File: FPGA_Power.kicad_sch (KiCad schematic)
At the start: 13 parts, among them U5 NCP115AMX120TCG, U9 ICE40UP5K-SG48ITR

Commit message: Fixed a lot more mistakes...
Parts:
- added TP28: 1V2, TestPoint:TestPoint_THTPad_D2.5mm_Drill1.2mm, symbol Connector:TestPoint
- U5: Price (none) -> $0.30
- U9: Price (none) -> $0.09
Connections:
- net +1V2: now also TP28.1
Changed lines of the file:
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@@
 			)
 		)
-		(property "Price" ""
+		(property "Price" "$0.30"
 			(at 111.76 86.36 0)
 			(hide yes)
@@
 			)
 		)
+		(property "Field21" ""
+			(at 111.76 86.36 0)
+			(hide yes)
+			(show_name no)
+			(do_not_autoplace no)
+			(effects
+				(font
+					(size 1.27 1.27)
+				)
+			)
+		)
 		(pin "1"
 		)
@@
 	)
 	(symbol
+		(lib_id "Connector:TestPoint")
+		(at 146.05 76.2 90)
+		(unit 1)
+		(body_style 1)
+		(exclude_from_sim no)
+		(in_bom yes)
+		(on_board yes)
+		(in_pos_files yes)
+		(dnp no)
+		(property "Reference" "TP28"
+			(at 139.7 76.2 90)
+			(hide yes)
+			(show_name no)
+			(do_not_autoplace no)
+			(effects
+				(font
+					(size 1.27 1.27)
+				)
+				(justify left)
+			)
+		)
+		(property "Value" "1V2"
+			(at 143.51 78.74 90)
+			(show_name no)
+			(do_not_autoplace no)
+			(effects
+				(font
+					(size 1.27 1.27)
+				)
+				(justify left)
+			)
+		)
+		(property "Footprint" "TestPoint:TestPoint_THTPad_D2.5mm_Drill1.2mm"
+			(at 146.05 71.12 0)
+			(hide yes)
+			(show_name no)
+			(do_not_autoplace no)
+			(effects
+				(font
+					(size 1.27 1.27)
+				)
+			)
+		)
+		(property "Datasheet" ""
+			(at 146.05 71.12 0)
+			(hide yes)
+			(show_name no)
+			(do_not_autoplace no)
+			(effects
+				(font
+					(size 1.27 1.27)
+				)
+			)
+		)
+		(property "Description" ""
+			(at 146.05 76.2 0)
+			(hide yes)
+			(show_name no)
+			(do_not_autoplace no)
+			(effects
+				(font
+					(size 1.27 1.27)
+				)
+			)
+		)
+		(property "JLCPCB #" ""
+			(at 146.05 76.2 0)
+			(hide yes)
+			(show_name no)
+			(do_not_autoplace no)
+			(effects
+				(font
+					(size 1.27 1.27)
+				)
+			)
+		)
+		(pin "1"
+		)
+		(instances
+			(project "DDC_SDR"
+				(path "/7dfef218-ca21-47b0-a8d3-67c7d55cb9d2/2ce56689-3987-4b0d-b06d-53c251a2345f"
+					(reference "TP28")
+					(unit 1)
+				)
+			)
+		)
+	)
+	(symbol
 		(lib_id "UPduino_v3.0:power_GND")
 		(at 182.88 100.33 0)
@@
 			)
 		)
-		(property "Price" ""
+		(property "Price" "$0.09"
 			(at 212.09 106.68 90)
 			(hide yes)

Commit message: Fixing more errors....
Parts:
- renumbered U9 to U7
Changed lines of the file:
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@@
 		(in_pos_files yes)
 		(dnp no)
-		(property "Reference" "U9"
+		(property "Reference" "U7"
 			(at 212.09 97.3582 90)
 			(show_name no)
@@
 			(project "DDC_SDR"
 				(path "/7dfef218-ca21-47b0-a8d3-67c7d55cb9d2/2ce56689-3987-4b0d-b06d-53c251a2345f"
-					(reference "U9")
+					(reference "U7")
 					(unit 4)
 				)

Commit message: Minor tweaks...
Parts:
- U7: Price $0.09 -> $8.49
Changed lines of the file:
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@@
 			)
 		)
-		(property "Price" "$0.09"
+		(property "Price" "$8.49"
 			(at 212.09 106.68 90)
 			(hide yes)

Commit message: Starting to place components
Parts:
- JP1: footprint (none) -> Jumper:SolderJumper-2_P1.3mm_Bridged_RoundedPad1.0x1.5mm
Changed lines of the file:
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@@
 			)
 		)
-		(property "Footprint" ""
+		(property "Footprint" "Jumper:SolderJumper-2_P1.3mm_Bridged_RoundedPad1.0x1.5mm"
 			(at 154.94 92.71 0)
 			(hide yes)

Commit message: AF DAC Some VDDA Placed
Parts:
- renumbered C62 to C70, C61 to C71, C54 to C72, C39 to C73, C60 to C74, C33 to C75, C51 to C76, C56 to C77, D5 to D8, JP1 to JP7, R12 to R54, TP28 to TP9, U5 to U11
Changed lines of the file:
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@@
 		(in_pos_files yes)
 		(dnp no)
-		(property "Reference" "#PWR092"
+		(property "Reference" "#PWR0138"
 			(at 185.42 90.17 0)
 			(hide yes)
@@
 			(project "DDC_SDR"
 				(path "/7dfef218-ca21-47b0-a8d3-67c7d55cb9d2/2ce56689-3987-4b0d-b06d-53c251a2345f"
-					(reference "#PWR092")
+					(reference "#PWR0138")
 					(unit 1)
 				)
@@
 		(dnp no)
 		(fields_autoplaced yes)
-		(property "Reference" "U5"
+		(property "Reference" "U11"
 			(at 111.76 77.47 0)
 			(show_name no)
@@
 			(project "DDC_SDR"
 				(path "/7dfef218-ca21-47b0-a8d3-67c7d55cb9d2/2ce56689-3987-4b0d-b06d-53c251a2345f"
-					(reference "U5")
+					(reference "U11")
 					(unit 1)
 				)
@@
 		(in_pos_files yes)
 		(dnp no)
-		(property "Reference" "#PWR097"
+		(property "Reference" "#PWR0139"
 			(at 223.52 114.3 0)
 			(hide yes)
@@
 			(project "DDC_SDR"
 				(path "/7dfef218-ca21-47b0-a8d3-67c7d55cb9d2/2ce56689-3987-4b0d-b06d-53c251a2345f"
-					(reference "#PWR097")
+					(reference "#PWR0139")
 					(unit 1)
 				)
@@
 		(dnp no)
 		(fields_autoplaced yes)
-		(property "Reference" "C33"
+		(property "Reference" "C75"
 			(at 176.53 77.4699 0)
 			(show_name no)
@@
 			(project "DDC_SDR"
 				(path "/7dfef218-ca21-47b0-a8d3-67c7d55cb9d2/2ce56689-3987-4b0d-b06d-53c251a2345f"
-					(reference "C33")
+					(reference "C75")
 					(unit 1)
 				)
@@
 		(in_pos_files yes)
 		(dnp no)
-		(property "Reference" "#PWR090"
+		(property "Reference" "#PWR0136"
 			(at 173.99 90.17 0)
 			(hide yes)
@@
 			(project "DDC_SDR"
 				(path "/7dfef218-ca21-47b0-a8d3-67c7d55cb9d2/2ce56689-3987-4b0d-b06d-53c251a2345f"
-					(reference "#PWR090")
+					(reference "#PWR0136")
 					(unit 1)
 				)
@@
 		(dnp no)
 		(fields_autoplaced yes)
-		(property "Reference" "C61"
+		(property "Reference" "C71"
 			(at 125.73 85.0899 0)
 			(show_name no)
@@
 			(project "DDC_SDR"
 				(path "/7dfef218-ca21-47b0-a8d3-67c7d55cb9d2/2ce56689-3987-4b0d-b06d-53c251a2345f"
-					(reference "C61")
+					(reference "C71")
 					(unit 1)
 				)
@@
 		(in_pos_files yes)
 		(dnp no)
-		(property "Reference" "#PWR085"
+		(property "Reference" "#PWR0133"
 			(at 157.48 130.81 0)
 			(hide yes)
@@
 			(project "DDC_SDR"
 				(path "/7dfef218-ca21-47b0-a8d3-67c7d55cb9d2/2ce56689-3987-4b0d-b06d-53c251a2345f"
-					(reference "#PWR085")
+					(reference "#PWR0133")
 					(unit 1)
 				)
@@
 		(dnp no)
 		(fields_autoplaced yes)
-		(property "Reference" "C54"
+		(property "Reference" "C72"
 			(at 160.02 118.1099 0)
 			(show_name no)
@@
 			(project "DDC_SDR"
 				(path "/7dfef218-ca21-47b0-a8d3-67c7d55cb9d2/2ce56689-3987-4b0d-b06d-53c251a2345f"
-					(reference "C54")
+					(reference "C72")
 					(unit 1)
 				)
@@
 		(dnp no)
 		(fields_autoplaced yes)
-		(property "Reference" "C62"
+		(property "Reference" "C70"
 			(at 99.06 92.7099 0)
 			(show_name no)
@@
 			(project "DDC_SDR"
 				(path "/7dfef218-ca21-47b0-a8d3-67c7d55cb9d2/2ce56689-3987-4b0d-b06d-53c251a2345f"
-					(reference "C62")
+					(reference "C70")
 					(unit 1)
 				)
@@
 		(in_pos_files yes)
 		(dnp no)
-		(property "Reference" "TP28"
+		(property "Reference" "TP9"
 			(at 139.7 76.2 90)
 			(hide yes)
@@
 			(project "DDC_SDR"
 				(path "/7dfef218-ca21-47b0-a8d3-67c7d55cb9d2/2ce56689-3987-4b0d-b06d-53c251a2345f"
-					(reference "TP28")
+					(reference "TP9")
 					(unit 1)
 				)
@@
 		(in_pos_files yes)
 		(dnp no)
-		(property "Reference" "#PWR091"
+		(property "Reference" "#PWR0137"
 			(at 182.88 106.68 0)
 			(hide yes)
@@
 			(project "DDC_SDR"
 				(path "/7dfef218-ca21-47b0-a8d3-67c7d55cb9d2/2ce56689-3987-4b0d-b06d-53c251a2345f"
-					(reference "#PWR091")
+					(reference "#PWR0137")
 					(unit 1)
 				)
@@
 		(in_pos_files yes)
 		(dnp no)
-		(property "Reference" "#PWR087"
+		(property "Reference" "#PWR0135"
 			(at 172.72 130.81 0)
 			(hide yes)
@@
 			(project "DDC_SDR"
 				(path "/7dfef218-ca21-47b0-a8d3-67c7d55cb9d2/2ce56689-3987-4b0d-b06d-53c251a2345f"
-					(reference "#PWR087")
+					(reference "#PWR0135")
 					(unit 1)
 				)
@@
 		(in_pos_files yes)
 		(dnp no)
-		(property "Reference" "#PWR014"
+		(property "Reference" "#PWR0128"
 			(at 96.52 105.41 0)
 			(hide yes)
@@
 			(project "DDC_SDR"
 				(path "/7dfef218-ca21-47b0-a8d3-67c7d55cb9d2/2ce56689-3987-4b0d-b06d-53c251a2345f"
-					(reference "#PWR014")
+					(reference "#PWR0128")
 					(unit 1)
 				)
@@
 		(dnp no)
 		(fields_autoplaced yes)
-		(property "Reference" "C39"
+		(property "Reference" "C73"
 			(at 175.26 93.9799 0)
 			(show_name no)
@@
 			(project "DDC_SDR"
 				(path "/7dfef218-ca21-47b0-a8d3-67c7d55cb9d2/2ce56689-3987-4b0d-b06d-53c251a2345f"
-					(reference "C39")
+					(reference "C73")
 					(unit 1)
 				)
@@
 		(dnp no)
 		(fields_autoplaced yes)
-		(property "Reference" "C56"
+		(property "Reference" "C77"
 			(at 187.96 77.4699 0)
 			(show_name no)
@@
 			(project "DDC_SDR"
 				(path "/7dfef218-ca21-47b0-a8d3-67c7d55cb9d2/2ce56689-3987-4b0d-b06d-53c251a2345f"
-					(reference "C56")
+					(reference "C77")
 					(unit 1)
 				)
@@
 		(dnp no)
 		(fields_autoplaced yes)
-		(property "Reference" "C51"
+		(property "Reference" "C76"
 			(at 185.42 93.9799 0)
 			(show_name no)
@@
 			(project "DDC_SDR"
 				(path "/7dfef218-ca21-47b0-a8d3-67c7d55cb9d2/2ce56689-3987-4b0d-b06d-53c251a2345f"
-					(reference "C51")
+					(reference "C76")
 					(unit 1)
 				)
@@
 		(in_pos_files yes)
 		(dnp no)
-		(property "Reference" "#PWR086"
+		(property "Reference" "#PWR0134"
 			(at 172.72 106.68 0)
 			(hide yes)
@@
 			(project "DDC_SDR"
 				(path "/7dfef218-ca21-47b0-a8d3-67c7d55cb9d2/2ce56689-3987-4b0d-b06d-53c251a2345f"
-					(reference "#PWR086")
+					(reference "#PWR0134")
 					(unit 1)
 				)
@@
 		(in_pos_files yes)
 		(dnp no)
-		(property "Reference" "#PWR0113"
+		(property "Reference" "#PWR0127"
 			(at 96.52 86.36 0)
 			(hide yes)
@@
 			(project "DDC_SDR"
 				(path "/7dfef218-ca21-47b0-a8d3-67c7d55cb9d2/2ce56689-3987-4b0d-b06d-53c251a2345f"
-					(reference "#PWR0113")
+					(reference "#PWR0127")
 					(unit 1)
 				)
@@
 		(dnp no)
 		(fields_autoplaced yes)
-		(property "Reference" "C60"
+		(property "Reference" "C74"
 			(at 175.26 118.1099 0)
 			(show_name no)
@@
 			(project "DDC_SDR"
 				(path "/7dfef218-ca21-47b0-a8d3-67c7d55cb9d2/2ce56689-3987-4b0d-b06d-53c251a2345f"
-					(reference "C60")
+					(reference "C74")
 					(unit 1)
 				)
@@
 		(in_pos_files yes)
 		(dnp no)
-		(property "Reference" "#PWR076"
+		(property "Reference" "#PWR0130"
 			(at 127 87.63 0)
 			(hide yes)
@@
 			(project "DDC_SDR"
 				(path "/7dfef218-ca21-47b0-a8d3-67c7d55cb9d2/2ce56689-3987-4b0d-b06d-53c251a2345f"
-					(reference "#PWR076")
+					(reference "#PWR0130")
 					(unit 1)
 				)
@@
 		(in_pos_files yes)
 		(dnp no)
-		(property "Reference" "D5"
+		(property "Reference" "D8"
 			(at 166.37 111.3282 0)
 			(show_name no)
@@
 			(project "DDC_SDR"
 				(path "/7dfef218-ca21-47b0-a8d3-67c7d55cb9d2/2ce56689-3987-4b0d-b06d-53c251a2345f"
-					(reference "D5")
+					(reference "D8")
 					(unit 1)
 				)
@@
 		(in_pos_files yes)
 		(dnp no)
-		(property "Reference" "R12"
+		(property "Reference" "R54"
 			(at 154.94 70.9422 90)
 			(show_name no)
@@
 			(project "DDC_SDR"
 				(path "/7dfef218-ca21-47b0-a8d3-67c7d55cb9d2/2ce56689-3987-4b0d-b06d-53c251a2345f"
-					(reference "R12")
+					(reference "R54")
 					(unit 1)
 				)
@@
 		(dnp no)
 		(fields_autoplaced yes)
-		(property "Reference" "JP1"
+		(property "Reference" "JP7"
 			(at 154.94 90.17 0)
 			(show_name no)
@@
 			(project "DDC_SDR"
 				(path "/7dfef218-ca21-47b0-a8d3-67c7d55cb9d2/2ce56689-3987-4b0d-b06d-53c251a2345f"
-					(reference "JP1")
+					(reference "JP7")
 					(unit 1)
 				)
@@
 		(in_pos_files yes)
 		(dnp no)
-		(property "Reference" "#PWR050"
+		(property "Reference" "#PWR0131"
 			(at 146.05 78.74 0)
 			(hide yes)
@@
 			(project "DDC_SDR"
 				(path "/7dfef218-ca21-47b0-a8d3-67c7d55cb9d2/2ce56689-3987-4b0d-b06d-53c251a2345f"
-					(reference "#PWR050")
+					(reference "#PWR0131")
 					(unit 1)
 				)
@@
 		(in_pos_files yes)
 		(dnp no)
-		(property "Reference" "#PWR034"
+		(property "Reference" "#PWR0129"
 			(at 111.76 100.33 0)
 			(hide yes)
@@
 			(project "DDC_SDR"
 				(path "/7dfef218-ca21-47b0-a8d3-67c7d55cb9d2/2ce56689-3987-4b0d-b06d-53c251a2345f"
-					(reference "#PWR034")
+					(reference "#PWR0129")
 					(unit 1)
 				)
@@
 		(in_pos_files yes)
 		(dnp no)
-		(property "Reference" "#PWR0111"
+		(property "Reference" "#PWR0132"
 			(at 152.4 120.65 0)
 			(hide yes)
@@
 			(project "DDC_SDR"
 				(path "/7dfef218-ca21-47b0-a8d3-67c7d55cb9d2/2ce56689-3987-4b0d-b06d-53c251a2345f"
-					(reference "#PWR0111")
+					(reference "#PWR0132")
 					(unit 1)
 				)

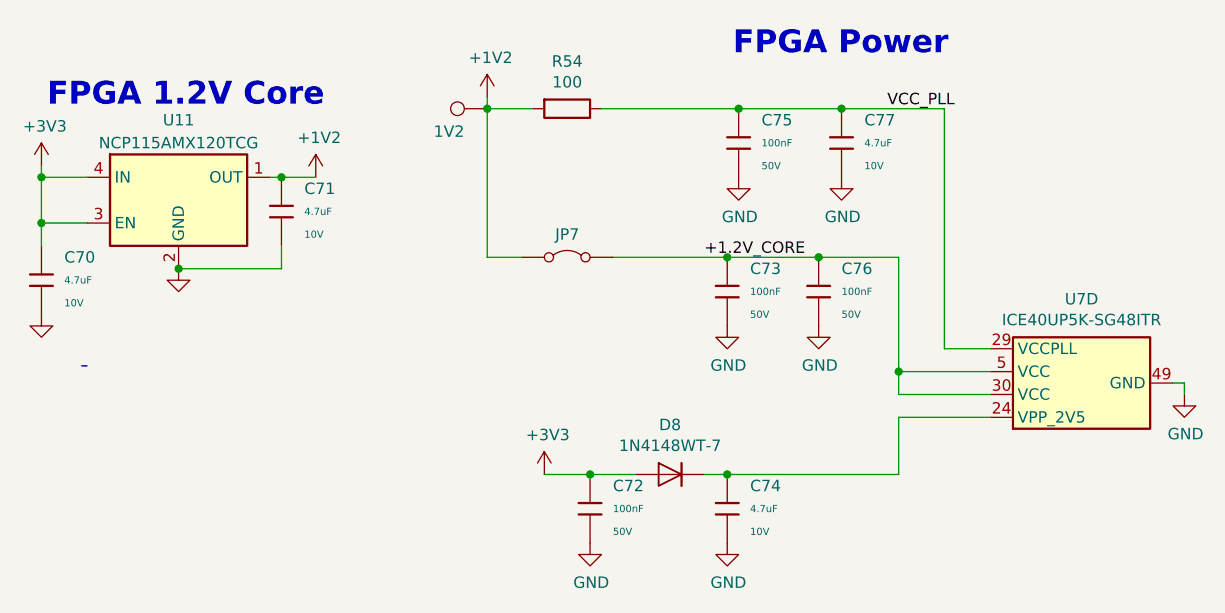
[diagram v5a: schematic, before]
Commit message: FPGA 1.2V placed
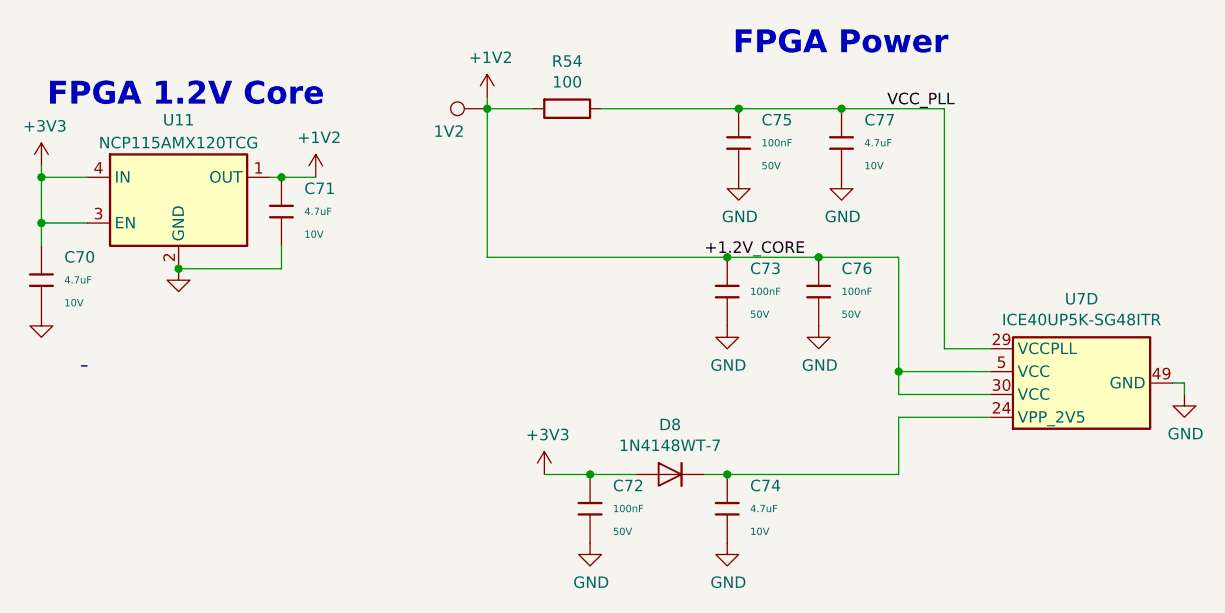
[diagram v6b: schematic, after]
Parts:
- removed JP7: Jumper_2_Bridged, Jumper:SolderJumper-2_P1.3mm_Bridged_RoundedPad1.0x1.5mm, symbol Jumper:Jumper_2_Bridged
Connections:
- net +1.2V_CORE is gone; now on net +1V2: C73.1, C76.1, U7.30 (VCC), U7.5 (VCC)
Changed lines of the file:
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@@
 	(wire
 		(pts
-			(xy 146.05 92.71) (xy 149.86 92.71)
-		)
-		(stroke
-			(width 0)
-			(type default)
-		)
-	)
-	(wire
-		(pts
-			(xy 160.02 92.71) (xy 172.72 92.71)
+			(xy 146.05 92.71) (xy 172.72 92.71)
 		)
 		(stroke
@@
 					(unit 1)
 				)
-			)
-		)
-	)
-	(symbol
-		(lib_id "Jumper:Jumper_2_Bridged")
-		(at 154.94 92.71 0)
-		(unit 1)
-		(body_style 1)
-		(exclude_from_sim no)
-		(in_bom yes)
-		(on_board yes)
-		(in_pos_files yes)
-		(dnp no)
-		(fields_autoplaced yes)
-		(property "Reference" "JP7"
-			(at 154.94 90.17 0)
-			(show_name no)
-			(do_not_autoplace no)
-			(effects
-				(font
-					(size 1.27 1.27)
-				)
-			)
-		)
-		(property "Value" "Jumper_2_Bridged"
-			(at 154.94 90.17 0)
-			(hide yes)
-			(show_name no)
-			(do_not_autoplace no)
-			(effects
-				(font
-					(size 1.27 1.27)
-				)
-			)
-		)
-		(property "Footprint" "Jumper:SolderJumper-2_P1.3mm_Bridged_RoundedPad1.0x1.5mm"
-			(at 154.94 92.71 0)
-			(hide yes)
-			(show_name no)
-			(do_not_autoplace no)
-			(effects
-				(font
-					(size 1.27 1.27)
-				)
-			)
-		)
-		(property "Datasheet" ""
-			(at 154.94 97.79 0)
-			(hide yes)
-			(show_name no)
-			(do_not_autoplace no)
-			(effects
-				(font
-					(size 1.27 1.27)
-				)
-			)
-		)
-		(property "Description" "Jumper, 2-pole, closed/bridged"
-			(at 154.94 100.33 0)
-			(hide yes)
-			(show_name no)
-			(do_not_autoplace no)
-			(effects
-				(font
-					(size 1.27 1.27)
-				)
-			)
-		)
-		(pin "1"
-		)
-		(pin "2"
-		)
-		(instances
-			(project "DDC_SDR"
-				(path "/7dfef218-ca21-47b0-a8d3-67c7d55cb9d2/2ce56689-3987-4b0d-b06d-53c251a2345f"
-					(reference "JP7")
-					(unit 1)
-				)

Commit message: Fixed schematic errors, all placed
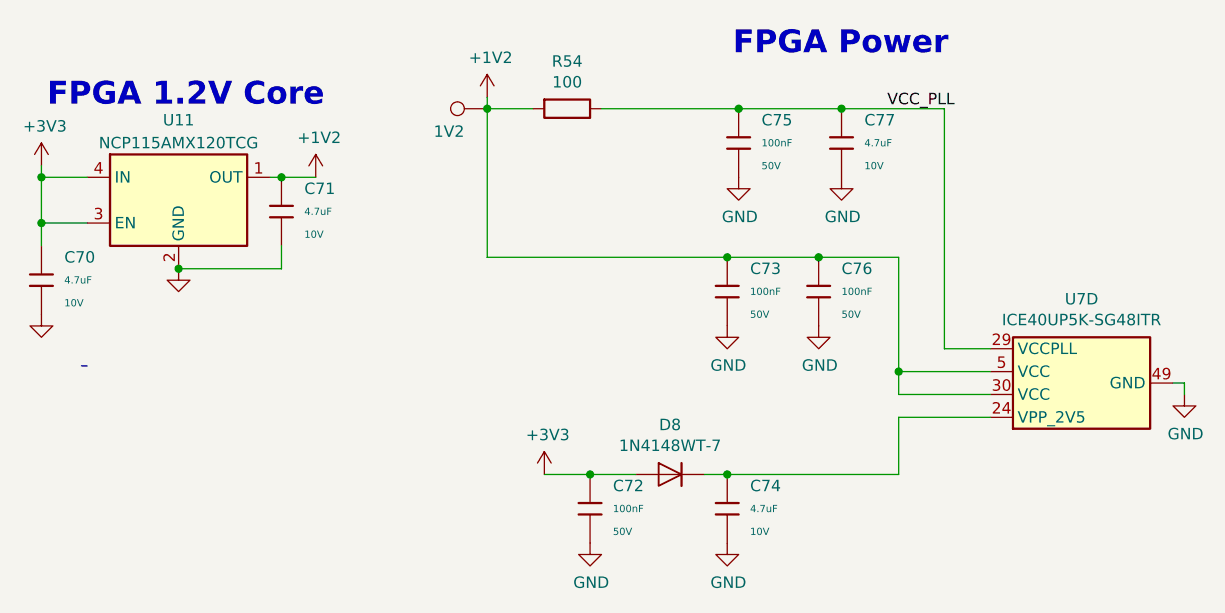
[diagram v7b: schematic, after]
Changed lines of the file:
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@@
-		)
-	)
-	(label "+1.2V_CORE"
-		(at 170.18 92.71 0)
-		(effects
-			(font
-				(size 1.27 1.27)
-			)
-			(justify left bottom)
 		)
 	)

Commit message: Added Prototype Area
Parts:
- TP9: footprint TestPoint:TestPoint_THTPad_D2.5mm_Drill1.2mm -> RP2040_minimal:TestPoint_THTPad_D2.5mm_Drill1.2mm
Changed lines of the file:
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@@
 			)
 		)
-		(property "Footprint" "TestPoint:TestPoint_THTPad_D2.5mm_Drill1.2mm"
+		(property "Footprint" "RP2040_minimal:TestPoint_THTPad_D2.5mm_Drill1.2mm"
 			(at 146.05 71.12 0)
 			(hide yes)
